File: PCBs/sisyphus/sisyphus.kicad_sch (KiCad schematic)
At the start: 66 parts, among them J1 USB_BOOT, J10 SPK, J2 SWD, J3 Battery, J4 USB_C_Receptacle_USB2.0_14P, J5 KEYB, J6 AUX, J9 RGB_CONN, Q1 AO3401A, SW1 SW_SPDT_321, U1 W25Q128JVS, U2 RP2040, U3 TPS62291, U4 BQ25619, U5 USBLC6-2P6, U6 TCA8418, U7 MAX98357A, Y1 ABM8-272-T3

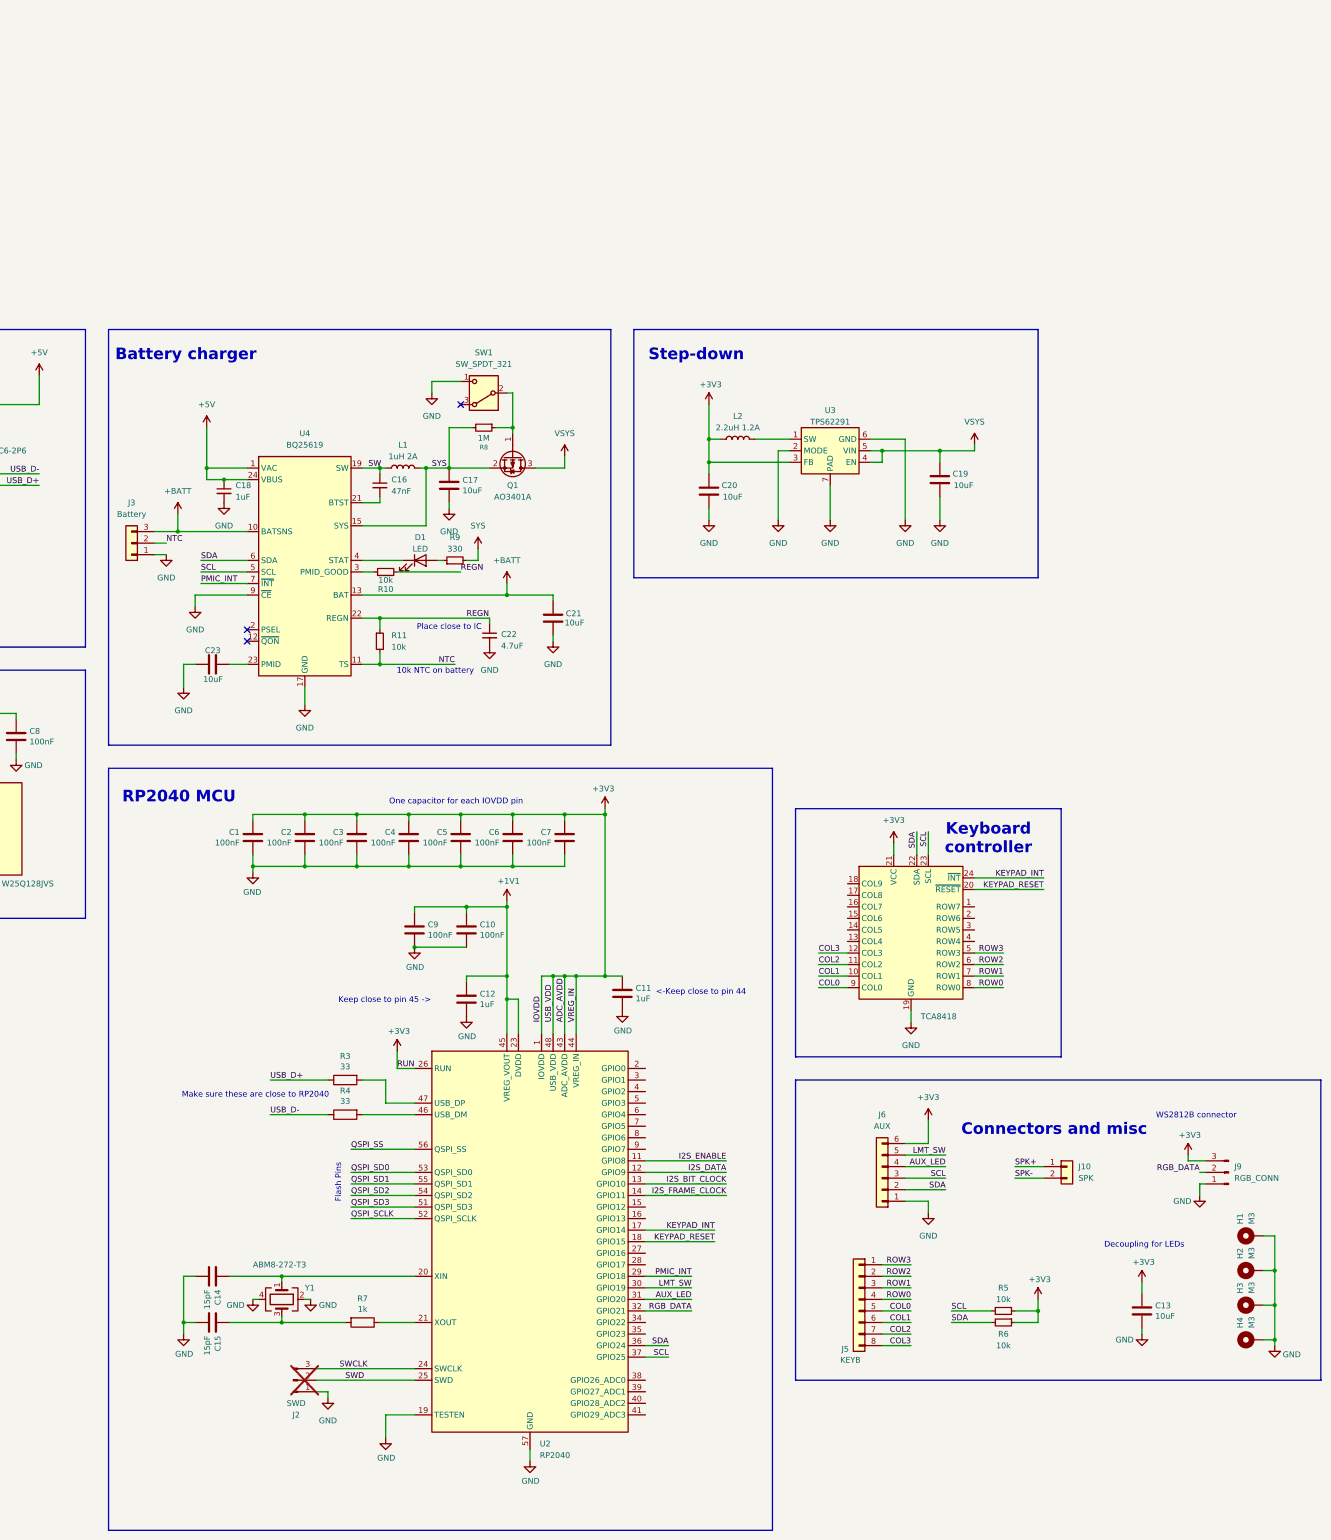
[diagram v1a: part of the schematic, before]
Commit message: Replace charger with normal one, Add fuel gauge
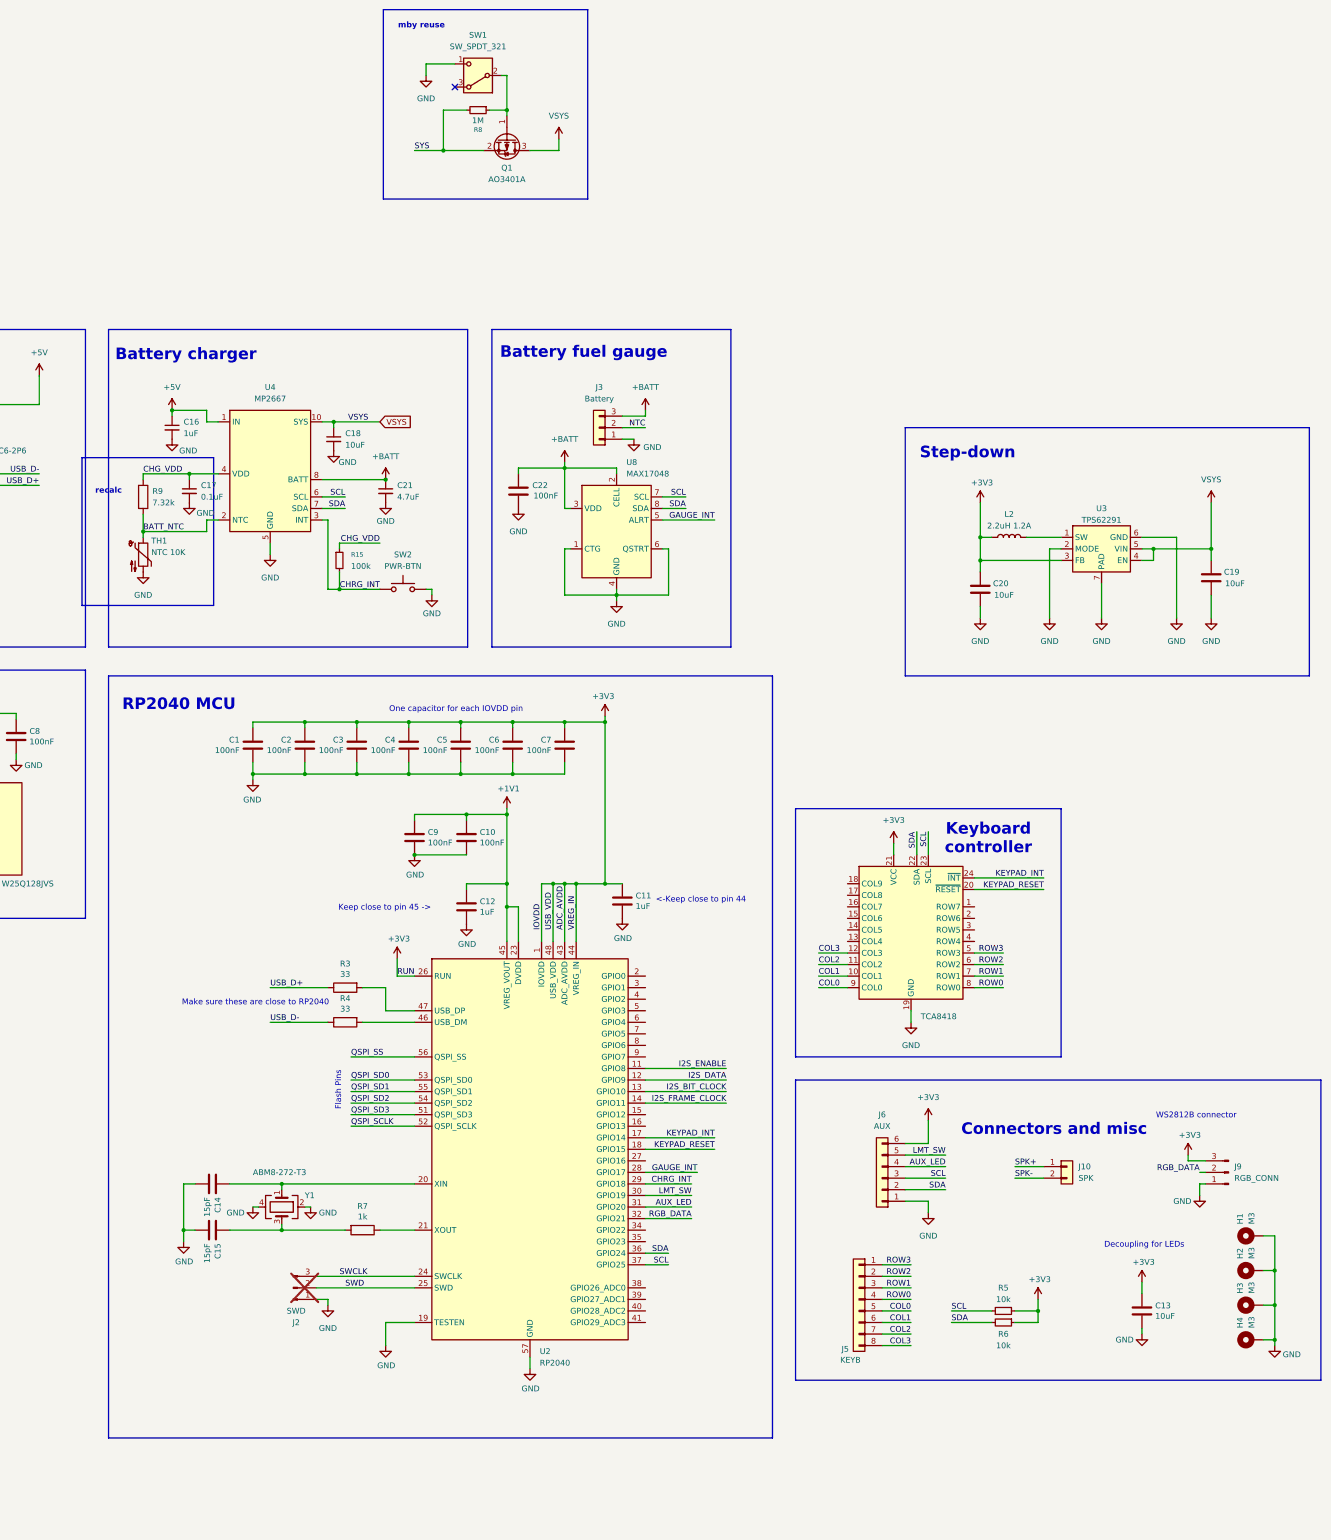
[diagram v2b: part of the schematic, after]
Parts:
- removed C17, C21, C23: 10uF, Capacitor_SMD:C_0402_1005Metric, symbol Device:C
- removed C22: 4.7uF, Capacitor_SMD:C_0402_1005Metric, symbol Device:C_Small
- removed D1: LED, LED_SMD:LED_0603_1608Metric, symbol Device:LED
- removed L1: 1uH 2A, Inductor_SMD:L_0603_1608Metric, symbol Device:L
- removed R10, R11: 10k, Resistor_SMD:R_0402_1005Metric, symbol Device:R_Small
- removed R9: 330, Resistor_SMD:R_0402_1005Metric, symbol Device:R_Small
- removed U4: BQ25619, Package_DFN_QFN:Texas_RTW_WQFN-24-1EP_4x4mm_P0.5mm_EP2.7x2.7mm_ThermalVias, symbol Sisyphus:BQ25619
- added C17: 0.1uF, Capacitor_SMD:C_0201_0603Metric, symbol Device:C_Small
- added C21: 4.7uF, Capacitor_SMD:C_0402_1005Metric, symbol Device:C_Small
- added C22: 100nF, Package_DFN_QFN:TDFN-8-1EP_2x2mm_P0.5mm_EP0.8x1.2mm, symbol Device:C
- added R15: 100k, Resistor_SMD:R_0201_0603Metric, symbol Device:R_Small
- added R9: 7.32k, Resistor_SMD:R_0201_0603Metric, symbol Device:R
- added SW2: PWR-BTN, Button_Switch_THT:SW_NKK_GW12LJP, symbol Switch:SW_Push
- added TH1: NTC 10K, symbol Device:Thermistor_NTC
- added U4: MP2667, sisyphus:MPS_MP2664_QFN-10_2x2mm_P0.5mm, symbol Sisyphus:MP2667
- added U8: MAX17048, Package_DFN_QFN:TDFN-8-1EP_2x2mm_P0.5mm_EP0.8x1.2mm, symbol Sisyphus:MAX17048
- C16: value 47nF -> 1uF; footprint Capacitor_SMD:C_0402_1005Metric -> Capacitor_SMD:C_0201_0603Metric; LCSC Part https://lcsc.com/product-detail/Multilayer-Ceramic-Capacito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 -> (none); LCSC_Part (none) -> C14445
- C18: value 1uF -> 10uF; 0204 (none) -> x; 0402 (none) -> x; LCSC_Part (none) -> C315248
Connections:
- net SW is gone; now on net +5V: C16.1
- net +5V: now also U4.1 (IN); no longer C18.1
- net +BATT: now also C21.1, C22.1, U4.8 (BATT), U4.9 (BATT), U8.2 (CELL), U8.3 (VDD)
- net GND: now also C16.2, C17.2, C21.2, C22.2, SW2.2, TH1.2, U4.5 (GND), U8.1 (CTG), U8.4 (GND), U8.6 (QSTRT)
- net SCL: now also U4.6 (SCL), U8.7 (SCL)
- net SDA: now also U4.7 (SDA), U8.8 (SDA)
- net VSYS: now also C18.1, U4.10 (SYS)
- net GAUGE_INT: now reaches U2.28 (GPIO17)
- net GAUGE_INT: now also U8.5 (ALRT)
- net PMIC_INT renamed CHRG_INT
- net CHRG_INT: now also R15.2, SW2.1, U4.3 (INT)
- new net BATT_NTC: R9.2, TH1.1, U4.2 (NTC)
- new net CHG_VDD: C17.1, R15.1, R9.1, U4.4 (VDD)
- no-connect marks 3 -> 1
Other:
- note added: "Battery fuel gauge"
- note added: "mby reuse"
- note added: "recalc"
- note removed: "10k NTC on battery"
- note removed: "Place close to IC"
- moved on the sheet: C1, C10, C11, C12, C14, C15, C19, C2, C20, C3, C4, C5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

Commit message: Put power switch back with a bypass
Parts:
- added JP2: PWR SW bypass, Jumper:SolderJumper-2_P1.3mm_Bridged2Bar_RoundedPad1.0x1.5mm, symbol Jumper:SolderJumper_2_Bridged
- Q1, R8, SW1: now not fitted
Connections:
- net SYS: now also C18.1, U4.10 (SYS), JP2.2 (B)
- net VSYS: now also JP2.1 (A); no longer C18.1, U4.10 (SYS)
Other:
- note added: "Power switch"
- note removed: "mby reuse"
- moved on the sheet: C19, C20, L2, U3

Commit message: Schematic refinements, start of PCB
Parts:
- removed J9: RGB_CONN, Connector_PinHeader_2.54mm:PinHeader_1x03_P2.54mm_Vertical, symbol Connector:Conn_01x03_Pin
- removed SW2: PWR-BTN, Button_Switch_THT:SW_NKK_GW12LJP, symbol Switch:SW_Push
- removed U1: W25Q128JVS, Package_SO:SOIC-8_5.23x5.23mm_P1.27mm, symbol Memory_Flash:W25Q128JVS
- added J5: RGB_CONN, Connector_JST:JST_PH_S3B-PH-SM4-TB_1x03-1MP_P2.00mm_Horizontal, symbol Connector_Generic_MountingPin:Conn_01x03_MountingPin
- added J9: PWR-BTN, Connector_JST:JST_PH_S2B-PH-SM4-TB_1x02-1MP_P2.00mm_Horizontal, symbol Connector_Generic_MountingPin:Conn_01x02_MountingPin
- added U5: W25Q128JVP, Package_SON:WSON-8-1EP_6x5mm_P1.27mm_EP3.4x4.3mm, symbol Memory_Flash:W25Q128JVP
- C1: renamed from C16; footprint Capacitor_SMD:C_0201_0603Metric -> Capacitor_SMD:C_0402_1005Metric
- C4: renamed from C17; footprint Capacitor_SMD:C_0201_0603Metric -> Capacitor_SMD:C_0402_1005Metric
- C6: renamed from C22; footprint Package_DFN_QFN:TDFN-8-1EP_2x2mm_P0.5mm_EP0.8x1.2mm -> Capacitor_SMD:C_0402_1005Metric
- J1: renamed from J3; symbol Connector_Generic:Conn_01x03 -> Connector_Generic_MountingPin:Conn_01x03_MountingPin
- J2: renamed from J4; symbol Connector:USB_C_Receptacle_USB2.0_14P -> Connector:USB_C_Receptacle_USB2.0_16P
- J4: renamed from J10; footprint Connector_PinHeader_2.54mm:PinHeader_1x02_P2.54mm_Vertical -> Connector_JST:JST_PH_S2B-PH-SM4-TB_1x02-1MP_P2.00mm_Horizontal; symbol Connector_Generic:Conn_01x02 -> Connector_Generic_MountingPin:Conn_01x02_MountingPin; now in the parts list
- J6: footprint (none) -> Connector_JST:JST_PH_S6B-PH-SM4-TB_1x06-1MP_P2.00mm_Horizontal; symbol Connector_Generic:Conn_01x06 -> Connector_Generic_MountingPin:Conn_01x06_MountingPin
- J8: renamed from J5; footprint Connector_JST:JST_XH_S8B-XH-A_1x08_P2.50mm_Horizontal -> Connector_JST:JST_PH_S8B-PH-SM4-TB_1x08-1MP_P2.00mm_Horizontal; symbol Connector_Generic:Conn_01x08 -> Connector_Generic_MountingPin:Conn_01x08_MountingPin; LCSC Part https://lcsc.com/product-detail/Wire-To-Board-Connector_JST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 -> (none)
- R2: renamed from R8; value 1M -> 330k
- R4: renamed from R9; footprint Resistor_SMD:R_0201_0603Metric -> Resistor_SMD:R_0402_1005Metric
- R5: renamed from R15; footprint Resistor_SMD:R_0201_0603Metric -> Resistor_SMD:R_0402_1005Metric
- renumbered C2 to C10, C3 to C11, C4 to C12, C5 to C13, C6 to C14, C7 to C15, C9 to C16, C10 to C17, C11 to C18, C12 to C19, C18 to C2, C24 to C20, C25 to C21, C14 to C22, C15 to C23, C13 to C24, C19 to C3, C21 to C5, C20 to C7, C1 to C9, D2 to D1, J1 to J3, J2 to J7, JP2 to JP1, JP1 to JP2, L2 to L1, R12 to R1, R14 to R10, R7 to R11, R5 to R12, R6 to R13, R13 to R3, R1 to R6, R2 to R7, R3 to R8, R4 to R9, U3 to U1, U4 to U2, U5 to U3, U8 to U4, U2 to U8
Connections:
- net +3V3: now also J5.3 (Pin_3), U5.8 (VCC)
- net +5V: no longer U3.5 (VBUS)
- net CHRG_INT: now also U8.5 (GPIO3), J9.1 (Pin_1); no longer U8.29 (GPIO18)
- net GAUGE_INT: now also U8.4 (GPIO2); no longer U8.28 (GPIO17)
- net GND: now also J1.MP (MountPin), J2.SH (SHIELD), J4.MP (MountPin), J6.MP (MountPin), J8.MP (MountPin), U4.9 (GND), J5.1 (Pin_1), J5.MP (MountPin), J9.2 (Pin_2), J9.MP (MountPin), U5.4 (GND), U5.9 (EP); no longer J2.S1 (SHIELD)
- net I2S_BIT_CLOCK: now also U8.36 (GPIO24); no longer U8.13 (GPIO10)
- net I2S_DATA: now also U8.35 (GPIO23); no longer U8.12 (GPIO9)
- net I2S_ENABLE: now also U8.34 (GPIO22); no longer U8.11 (GPIO8)
- net I2S_FRAME_CLOCK: now also U8.37 (GPIO25); no longer U8.14 (GPIO11)
- net KEYPAD_INT: now also U8.15 (GPIO12); no longer U8.17 (GPIO14)
- net KEYPAD_RESET: now also U8.16 (GPIO13); no longer U8.18 (GPIO15)
- net QSPI_SCLK: now also U5.6 (CLK)
- net QSPI_SD0: now also U5.5 (DI/IO_{0})
- net QSPI_SD1: now also U5.2 (DO/IO_{1})
- net QSPI_SD2: now also U5.3 (~{WP}/IO_{2})
- net QSPI_SD3: now also U5.7 (~{HOLD}/~{RESET}/IO_{3})
- net QSPI_SS: now also U5.1 (~{CS})
- net RGB_DATA: now also U8.6 (GPIO4), J5.2 (Pin_2); no longer U8.32 (GPIO21)
- net SCL: now also U8.3 (GPIO1); no longer U8.37 (GPIO25)
- net SDA: now also U8.2 (GPIO0); no longer U8.36 (GPIO24)
- net VBUS: now also U3.5 (VBUS)
- no-connect marks 1 -> 3
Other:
- note added: "maybe decouple?"
- moved on the sheet: C3, C7, D1, J3, L1, R6, R7, U1, U3

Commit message: PCB tweaks
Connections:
- net NTC is gone; now on net BATT_NTC: J1.2 (Pin_2)
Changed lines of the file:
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@@
 	(wire
 		(pts
-			(xy 227.33 34.29) (xy 227.33 35.56)
+			(xy 232.41 34.29) (xy 232.41 35.56)
 		)
 		(stroke
@@
 	(wire
 		(pts
-			(xy 224.79 40.64) (xy 222.25 40.64)
+			(xy 232.41 40.64) (xy 222.25 40.64)
 		)
 		(stroke
@@
 	(wire
 		(pts
-			(xy 222.25 38.1) (xy 227.33 38.1)
+			(xy 222.25 38.1) (xy 232.41 38.1)
 		)
 		(stroke
@@
 	(wire
 		(pts
-			(xy 222.25 35.56) (xy 227.33 35.56)
+			(xy 222.25 35.56) (xy 232.41 35.56)
 		)
 		(stroke
@@
 		)
 	)
-	(label "NTC"
-		(at 227.33 38.1 180)
+	(label "BATT_NTC"
+		(at 232.41 38.1 180)
 		(effects
 			(font
@@
 	(symbol
 		(lib_id "power:+BATT")
-		(at 227.33 34.29 0)
+		(at 232.41 34.29 0)
 		(unit 1)
 		(body_style 1)
@@
 		(fields_autoplaced yes)
 		(property "Reference" "#PWR07"
-			(at 227.33 38.1 0)
+			(at 232.41 38.1 0)
 			(hide yes)
 			(show_name no)
@@
 		)
 		(property "Value" "+BATT"
-			(at 227.33 29.21 0)
+			(at 232.41 29.21 0)
 			(show_name no)
 			(do_not_autoplace no)
@@
 		)
 		(property "Footprint" ""
-			(at 227.33 34.29 0)
+			(at 232.41 34.29 0)
 			(hide yes)
 			(show_name no)
@@
 		)
 		(property "Datasheet" ""
-			(at 227.33 34.29 0)
+			(at 232.41 34.29 0)
 			(hide yes)
 			(show_name no)
@@
 		)
 		(property "Description" "Power symbol creates a global label with name \"+BATT\""
-			(at 227.33 34.29 0)
+			(at 232.41 34.29 0)
 			(hide yes)
 			(show_name no)
@@
 	(symbol
 		(lib_id "power:GND")
-		(at 224.79 40.64 0)
+		(at 232.41 40.64 0)
 		(unit 1)
 		(body_style 1)
@@
 		(dnp no)
 		(property "Reference" "#PWR010"
-			(at 224.79 46.99 0)
+			(at 232.41 46.99 0)
 			(hide yes)
 			(show_name no)
@@
 		)
 		(property "Value" "GND"
-			(at 228.854 42.418 0)
+			(at 236.474 42.418 0)
 			(show_name no)
 			(do_not_autoplace no)
@@
 		)
 		(property "Footprint" ""
-			(at 224.79 40.64 0)
+			(at 232.41 40.64 0)
 			(hide yes)
 			(show_name no)
@@
 		)
 		(property "Datasheet" ""
-			(at 224.79 40.64 0)
+			(at 232.41 40.64 0)
 			(hide yes)
 			(show_name no)
@@
 		)
 		(property "Description" "Power symbol creates a global label with name \"GND\" , ground"
-			(at 224.79 40.64 0)
+			(at 232.41 40.64 0)
 			(hide yes)
 			(show_name no)

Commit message: PCB roated, far from perfect
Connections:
- net AUX_LED: now also U8.16 (GPIO13); no longer U8.31 (GPIO20)
- net KEYPAD_INT: now also U8.30 (GPIO19); no longer U8.15 (GPIO12)
- net KEYPAD_RESET: now also U8.31 (GPIO20); no longer U8.16 (GPIO13)
- net LMT_SW: now also U8.15 (GPIO12); no longer U8.30 (GPIO19)
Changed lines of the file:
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@@
 	(wire
 		(pts
-			(xy 227.33 189.23) (xy 242.57 189.23)
+			(xy 227.33 207.01) (xy 242.57 207.01)
 		)
 		(stroke
@@
 	(wire
 		(pts
-			(xy 227.33 191.77) (xy 242.57 191.77)
+			(xy 227.33 209.55) (xy 242.57 209.55)
 		)
 		(stroke
@@
 	(wire
 		(pts
-			(xy 227.33 207.01) (xy 237.49 207.01)
+			(xy 227.33 189.23) (xy 237.49 189.23)
 		)
 		(stroke
@@
 	(wire
 		(pts
-			(xy 227.33 209.55) (xy 237.49 209.55)
+			(xy 227.33 191.77) (xy 237.49 191.77)
 		)
 		(stroke
@@
 	)
 	(label "AUX_LED"
-		(at 237.49 209.55 180)
+		(at 237.49 191.77 180)
 		(effects
 			(font
@@
 	)
 	(label "KEYPAD_RESET"
-		(at 242.57 191.77 180)
+		(at 242.57 209.55 180)
 		(effects
 			(font
@@
 	)
 	(label "KEYPAD_INT"
-		(at 242.57 189.23 180)
+		(at 242.57 207.01 180)
 		(effects
 			(font
@@
 	)
 	(label "LMT_SW"
-		(at 237.49 207.01 180)
+		(at 237.49 189.23 180)
 		(effects
 			(font
